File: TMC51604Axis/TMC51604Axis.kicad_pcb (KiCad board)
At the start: 4 copper layers, 77.7 x 72.8 mm, 162 parts, among them J1 +48Vin, J2 Stepper_conn, J3 RJ45_Shielded, J4 EncCon1, J5 RJ45_Shielded, J6 EncCon2, Q1 SUD08P06-155L, Q2 DMHT6016LFJ, Q3 DMHT6016LFJ, Q4 BSS138, U1 AP2210-3.3V, U2 LM2937, U3 TMC5160A-TA, U4 ASDMB-12.0MHz, U5 74LVC125, U6 74LVC125, U7 74LVC125

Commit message: First layout V2
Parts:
- removed C21, C39: 220uF/100V, Capacitor_SMD:CP_Elec_10x14.3
- removed C44, C45: 100n, peters:C_0805_peter
- removed D15: LED, peters:D_0805__HandSolder_peter
- removed D21, D22, D23, D24, D26, D29: BAT54S, Package_TO_SOT_SMD:SOT-23
- removed F1: Fuse, Fuse:Fuse_2512_6332Metric
- removed R47: 2k2, peters:R_0805_peter
- removed R49: 100R, peters:R_0805_peter
- removed R50: 20R, peters:R_0805_peter
- removed R51, R52: 0R1, Resistor_SMD:R_1206_3216Metric
- removed TP1, TP2: TestPoint, TestPoint:TestPoint_Pad_D1.5mm
- removed U6: 74LVC125, Package_SO:SO-14_5.3x10.2mm_P1.27mm
- added C50: 470n/100V, Capacitor_SMD:C_1206_3216Metric, F.Cu at (111.4, 116.5)
- added C51: 470n/100V, Capacitor_SMD:C_1206_3216Metric, F.Cu at (98.0, 116.5)
- added C52: 330uF/100V, Capacitor_THT:CP_Radial_D12.5mm_P5.00mm, F.Cu at (116.8, 126.9)
- added C53: 330uF/100V, Capacitor_THT:CP_Radial_D12.5mm_P5.00mm, F.Cu at (82.3, 113.9)
- added C54: 330uF/100V, Capacitor_THT:CP_Radial_D12.5mm_P5.00mm, F.Cu at (116.8, 113.6)
- added C55: 330uF/100V, Capacitor_THT:CP_Radial_D12.5mm_P5.00mm, F.Cu at (82.3, 127.3)
- added J7: Stepper_conn, Connector_Phoenix_MSTB:PhoenixContact_MSTBA_2,5_4-G-5,08_1x04_P5.08mm_Horizontal, F.Cu at (91.6, 124.5)
- added Q5: SQJ481EP, Libs:PowerPAK SO-8L SINGLE, B.Cu at (73.4, 121.8)
- added R53: 47K, Resistor_SMD:R_0603_1608Metric, B.Cu at (100.9, 85.6)
- added R54: 47K, Resistor_SMD:R_0603_1608Metric, B.Cu at (102.4, 85.6)
- added REF**: OSHW-Logo2_7.3x6mm_Copper, Symbol:OSHW-Logo2_7.3x6mm_Copper, F.Cu at (130.2, 117.2)
- C13, C14, D20, D25, D27, D28, R6: moved to F.Cu
- C15, C16: footprint Capacitor_SMD:C_1210_3225Metric_Pad1.42x2.65mm_HandSolder -> Capacitor_SMD:C_1210_3225Metric_Pad1.33x2.70mm_HandSolder; moved to B.Cu
- C18: footprint peters:C_0805_peter -> Capacitor_SMD:C_0603_1608Metric
- C19, C26, C27, D3, R10, R11, R13, R14, R22, R23, R24, R25, R3, R7, R8: moved to B.Cu
- C2: value 10p -> 100n; footprint peters:C_0805_peter -> Capacitor_SMD:C_0603_1608Metric; moved to B.Cu
- C20, C38: value 470n/100V -> 470n/100V x2
- C23: value 2.2uF -> 2.2uFto10uF
- C25: value 2.2u -> 2.2uFto10uF; moved to B.Cu
- C3, C4: footprint Capacitor_SMD:CP_Elec_8x6.2 -> Capacitor_SMD:CP_Elec_8x10
- C37: footprint peters:C_0805_peter -> peters:D_0805_peter
- C5: value 47nF -> 100n; footprint peters:C_0805_peter -> Capacitor_SMD:C_0603_1608Metric; moved to B.Cu
- C8: footprint Capacitor_SMD:C_2010_5025Metric_Pad1.52x2.65mm_HandSolder -> Capacitor_SMD:C_1210_3225Metric_Pad1.33x2.70mm_HandSolder
- D11, D12, D13, D14, D16, D17, D18, D19: value LED -> BAT54S; footprint peters:D_0805__HandSolder_peter -> Package_TO_SOT_SMD:SOT-23
- D6: value D_Schottky -> SS34FA
- FB2: footprint Resistor_SMD:R_0805_2012Metric_Pad1.15x1.40mm_HandSolder -> Resistor_SMD:R_0805_2012Metric_Pad1.20x1.40mm_HandSolder
- J3: value RJ45_Shielded -> RJ45_STEP_DIR
- J5: value RJ45_Shielded -> RJ45_SPI
- JP1, JP2: footprint Jumper:SolderJumper-3_P2.0mm_Open_TrianglePad1.0x1.5mm -> Jumper:SolderJumper-3_P1.3mm_Bridged12_RoundedPad1.0x1.5mm
- Q1: value SUD08P06-155L -> BSS138; footprint Package_TO_SOT_SMD:TO-252-2 -> Package_TO_SOT_SMD:SOT-23
- Q2, Q3: value DMHT6016LFJ -> DMHT6016LFJ-Peters; footprint Libs:V-DFN5045-12 -> Libs:V-DFN5045-12 (Type B)
- R1: value 0R01 -> 100R; footprint Resistor_SMD:R_2512_6332Metric -> peters:R_0805_peter; moved to B.Cu
- R16, R27: value 0R1 -> 0R05; footprint Resistor_SMD:R_1206_3216Metric -> Resistor_SMD:R_2512_6332Metric_Pad1.40x3.35mm_HandSolder
- R19: footprint peters:R_0805_peter -> Resistor_SMD:R_0603_1608Metric
- R31, R32: value 2k2 -> 100R; moved to B.Cu
- R41: value 2k2 -> R; footprint peters:R_0805_peter -> peters:C_0805_peter; moved to B.Cu
- R42, R43, R44: value 2k2 -> 100K; footprint peters:R_0805_peter -> Resistor_SMD:R_0603_1608Metric
- R45, R46: value 2k2 -> 10K; footprint peters:R_0805_peter -> Resistor_SMD:R_0603_1608Metric
- TP4, TP5, TP6: footprint TestPoint:TestPoint_Pad_1.5x1.5mm -> TestPoint:TestPoint_THTPad_D1.0mm_Drill0.5mm
- U7: value 74LVC125 -> TXB0108PWR; footprint Package_SO:SO-14_5.3x10.2mm_P1.27mm -> digikey-footprints:TSSOP-20_W4.4mm
- moved H4 95.9 mm to (134.6, 65.2)
- moved JP1 80.9 mm to (73.3, 66.1), turned to 0 degrees
- moved H3 70.4 mm to (64.0, 65.2)
- moved R39 70.4 mm to (127.0, 74.7), turned to 0 degrees
- moved JP2 69.3 mm to (84.3, 66.1), turned to 0 degrees
- moved JP3 66.7 mm to (95.4, 66.1)
- moved J3 66.4 mm to (133.1, 97.2)
- moved J4 66.3 mm to (109.8, 66.3)
- moved J6 66.2 mm to (121.3, 66.3)
- moved J5 66.1 mm to (133.2, 78.1)
- moved H1 65.8 mm to (63.9, 131.0)
- moved C42 62.1 mm to (98.8, 65.5), turned to 180 degrees
- moved R38 60.9 mm to (110.0, 69.6), turned to 90 degrees
- moved C46 60.0 mm to (126.8, 105.3), turned to 180 degrees
- moved R48 59.6 mm to (114.3, 69.6)
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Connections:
- net Net-(C32-Pad1) renamed /MotorDrv1/SRB-
- net Net-(C32-Pad2) renamed /MotorDrv1/SRB+
- net Net-(C40-Pad1) renamed /MotorDrv1/SRA-
- net Net-(C40-Pad2) renamed /MotorDrv1/SRA+
- C2 pad 1: +48V -> GND
- C2 pad 2: Net-(C2-Pad2) -> VBUS
- C5 pad 1: Net-(C2-Pad2) -> GND
- C5 pad 2: GND -> +3V3
- D11 pad 2: Net-(D11-Pad2) -> VBUS
- D12 pad 2: Net-(D12-Pad2) -> VBUS
- D13 pad 2: Net-(D13-Pad2) -> VBUS
- D14 pad 2: Net-(D14-Pad2) -> VBUS
- D16 pad 1: Net-(D16-Pad1) -> GND
- D16 pad 2: /Inputs/DIR_REFR -> VBUS
- D17 pad 1: Net-(D17-Pad1) -> GND
- D17 pad 2: /MotorDrv1/REFL_STEP -> VBUS
- D18 pad 1: Net-(D18-Pad1) -> GND
- D18 pad 2: Net-(D18-Pad2) -> VBUS
- D19 pad 1: Net-(D19-Pad1) -> GND
- D19 pad 2: Net-(D19-Pad2) -> VBUS
- D20 pad 2: /Inputs/Signal_VCC -> VBUS
- D20 pad 3: Net-(D20-Pad3) -> /Inputs/SCK_raw
- D25 pad 3: Net-(D25-Pad3) -> /Inputs/ENC_A_raw
- D27 pad 3: Net-(D27-Pad3) -> /Inputs/ENC_B_raw
- D28 pad 3: Net-(D28-Pad3) -> /Inputs/ENC_N_raw
- D3 pad 1: Net-(C2-Pad2) -> +48V
- D5 pad 13: (no net) -> Net-(D5-Pad13)
- D5 pad 15: (no net) -> Net-(D5-Pad15)
- D5 pad 3: (no net) -> Net-(D5-Pad3)
- D5 pad 5: (no net) -> Net-(D5-Pad5)
- D5 pad 7: (no net) -> Net-(D5-Pad7)
- J2 pad 1: /MotorDrv1/StepperA -> /MotorDrv1/StepperD
- J2 pad 2: /MotorDrv1/StepperB -> /MotorDrv1/StepperC
- J2 pad 3: /MotorDrv1/StepperC -> /MotorDrv1/StepperB
- J2 pad 4: /MotorDrv1/StepperD -> /MotorDrv1/StepperA
- J3 pad 1: GND -> Net-(J3-Pad1)
- J3 pad 3: GND -> Net-(J3-Pad3)
- J3 pad 4: Net-(J3-Pad4) -> GND
- J3 pad 5: GND -> Net-(J3-Pad5)
- J3 pad 6: Net-(J3-Pad6) -> GND
- J3 pad 7: GND -> Net-(J3-Pad7)
- J3 pad 8: Net-(J3-Pad8) -> VBUS
- J4 pad 1: /Inputs/ENC_B_raw -> Net-(J4-Pad1)
- J4 pad 2: /Inputs/ENC_A_raw -> Net-(J4-Pad2)
- J5 pad 1: GND -> Net-(J5-Pad1)
- J5 pad 2: /Inputs/CSN_raw -> GND
- J5 pad 3: GND -> Net-(J5-Pad3)
- J5 pad 4: /Inputs/SDI_raw -> GND
- J5 pad 5: GND -> Net-(J5-Pad5)
- J5 pad 6: /Inputs/SDO_raw -> GND
- J5 pad 7: GND -> Net-(J5-Pad7)
- J5 pad 8: /Inputs/SCK_raw -> GND
- J6 pad 3: /Inputs/ENC_N_raw -> Net-(J6-Pad3)
- JP1 pad 1: GND -> +3V3
- JP1 pad 2: Net-(JP1-Pad2) -> /MotorDrv1/SPI_MODE
- JP1 pad 3: +3V3 -> GND
- JP2 pad 1: GND -> +3V3
- JP2 pad 2: Net-(JP2-Pad2) -> /MotorDrv1/SD_MODE
- JP2 pad 3: +3V3 -> GND
- Q1 pad 1: Net-(D3-Pad2) -> Net-(Q1-Pad1)
- Q1 pad 2: Net-(F1-Pad1) -> GND
- Q1 pad 3: Net-(C2-Pad2) -> Net-(Q1-Pad3)
- Q2 pad 10: /MotorDrv1/StepperB -> /MotorDrv1/StepperD
- Q2 pad 14: /MotorDrv1/StepperA -> /MotorDrv1/StepperC
- Q2 pad 15: /MotorDrv1/StepperB -> /MotorDrv1/StepperD
- Q2 pad 3: /MotorDrv1/StepperA -> /MotorDrv1/StepperC
- Q2 pad 5: Net-(C33-Pad2) -> Net-(C41-Pad2)
- Q2 pad 6: Net-(C33-Pad2) -> Net-(C41-Pad2)
- Q2 pad 7: Net-(C33-Pad2) -> Net-(C41-Pad2)
- Q2 pad 8: Net-(C33-Pad2) -> Net-(C41-Pad2)
- Q3 pad 10: /MotorDrv1/StepperD -> /MotorDrv1/StepperB
- Q3 pad 14: /MotorDrv1/StepperC -> /MotorDrv1/StepperA
- Q3 pad 15: /MotorDrv1/StepperD -> /MotorDrv1/StepperB
- Q3 pad 3: /MotorDrv1/StepperC -> /MotorDrv1/StepperA
- Q3 pad 5: Net-(C41-Pad2) -> Net-(C33-Pad2)
- Q3 pad 6: Net-(C41-Pad2) -> Net-(C33-Pad2)
- Q3 pad 7: Net-(C41-Pad2) -> Net-(C33-Pad2)
- Q3 pad 8: Net-(C41-Pad2) -> Net-(C33-Pad2)
- Q4 pad 2: GND -> Net-(Q1-Pad3)
- R1 pad 1: Net-(C2-Pad2) -> /Inputs/DIR_raw
- R1 pad 2: +48V -> Net-(J3-Pad7)
- R10 pad 2: Net-(Q2-Pad1) -> Net-(Q3-Pad1)
- R11 pad 1: Net-(Q2-Pad12) -> Net-(Q3-Pad12)
- R13 pad 2: Net-(Q2-Pad4) -> Net-(Q3-Pad4)
- R14 pad 1: Net-(Q2-Pad9) -> Net-(Q3-Pad9)
- R22 pad 2: Net-(Q3-Pad1) -> Net-(Q2-Pad1)
- R23 pad 1: Net-(Q3-Pad12) -> Net-(Q2-Pad12)
- R24 pad 2: Net-(Q3-Pad4) -> Net-(Q2-Pad4)
- R25 pad 1: Net-(Q3-Pad9) -> Net-(Q2-Pad9)
- R31 pad 1: /MotorDrv1/CLK -> /Inputs/Step_Raw
- R31 pad 2: Net-(D11-Pad2) -> Net-(J3-Pad5)
- R32 pad 1: /MotorDrv1/MOSI -> /MotorDrv1/DRV_ENA
- R32 pad 2: Net-(D12-Pad2) -> Net-(J3-Pad3)
- R33 pad 1: Net-(D20-Pad3) -> /Inputs/DIAG1_SWp_OUT
- R33 pad 2: Net-(J3-Pad4) -> Net-(J3-Pad2)
- R34 pad 1: Net-(D21-Pad3) -> /Inputs/DIAG0_SWn_OUT
- R34 pad 2: /Inputs/SDO_raw -> Net-(J3-Pad1)
- R35 pad 1: Net-(D22-Pad3) -> /Inputs/SCK_raw
- R35 pad 2: /Inputs/CSN_raw -> Net-(J5-Pad7)
- R36 pad 1: Net-(D23-Pad3) -> /Inputs/SDO_raw
- R36 pad 2: /Inputs/SDI_raw -> Net-(J5-Pad5)
- R37 pad 1: Net-(D24-Pad3) -> /Inputs/SDI_raw
- R37 pad 2: /Inputs/SCK_raw -> Net-(J5-Pad3)
- R38 pad 1: Net-(D25-Pad3) -> /Inputs/ENC_B_raw
- R38 pad 2: /Inputs/ENC_A_raw -> Net-(J4-Pad1)
- R39 pad 1: Net-(D26-Pad3) -> /Inputs/CSN_raw
- R39 pad 2: Net-(J3-Pad8) -> Net-(J5-Pad1)
- R40 pad 1: Net-(D27-Pad3) -> Net-(J4-Pad2)
- R40 pad 2: /Inputs/ENC_B_raw -> /Inputs/ENC_A_raw
- R41 pad 1: /Inputs/CSN -> Net-(R41-Pad1)
- R41 pad 2: Net-(D13-Pad2) -> GND
- R42 pad 1: /MotorDrv1/MISO -> Net-(Q1-Pad1)
- R42 pad 2: Net-(D14-Pad2) -> +12V
- R43 pad 1: Net-(D15-Pad1) -> GND
- R43 pad 2: GND -> Net-(Q1-Pad1)
- R44 pad 1: Net-(D16-Pad1) -> +3V3
- R44 pad 2: GND -> Net-(Q1-Pad3)
- R45 pad 1: Net-(D17-Pad1) -> +3V3
- R45 pad 2: GND -> /Inputs/DIR_REFR
- R46 pad 1: Net-(D18-Pad1) -> +3V3
- R46 pad 2: GND -> /MotorDrv1/REFL_STEP
- R48 pad 1: Net-(D28-Pad3) -> Net-(J6-Pad3)
- U3 pad 15: /MotorDrv1/MOSI -> /Inputs/SDI
- U3 pad 16: /MotorDrv1/MISO -> /Inputs/SDO
- U3 pad 21: Net-(JP1-Pad2) -> /MotorDrv1/SD_MODE
- U3 pad 22: Net-(JP2-Pad2) -> /MotorDrv1/SPI_MODE
- U3 pad 26: /MotorDrv1/DIAG0_SWn -> /Inputs/DIAG0_SWn
- U3 pad 27: /MotorDrv1/DIAG1_SWp -> /Inputs/DIAG1_SWp
- U5 pad 11: Net-(D19-Pad2) -> (no net)
- U5 pad 12: /MotorDrv1/DIAG0_SWn -> (no net)
- U5 pad 13: GND -> (no net)
- U7 pad 1: GND -> /Inputs/DIAG1_SWp
- U7 pad 10: GND -> Net-(R41-Pad1)
- U7 pad 11: Net-(D18-Pad2) -> GND
- U7 pad 12: /MotorDrv1/DIAG1_SWp -> /Inputs/SCK_raw
- U7 pad 13: GND -> /Inputs/SDO_raw
- U7 pad 14: +3V3 -> /Inputs/SDI_raw
- U7 pad 2: Net-(D20-Pad3) -> +3V3
- U7 pad 3: /MotorDrv1/DRV_ENA -> /Inputs/DIAG0_SWn
- U7 pad 4: GND -> /MotorDrv1/REFL_STEP
- U7 pad 5: Net-(D26-Pad3) -> /Inputs/DIR_REFR
- U7 pad 6: /Inputs/DIR_REFR -> /Inputs/CSN
- U7 pad 7: GND -> /Inputs/SDI
- U7 pad 8: /MotorDrv1/REFL_STEP -> /Inputs/SDO
- U7 pad 9: Net-(D29-Pad3) -> /MotorDrv1/CLK
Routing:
- net GND: track 353.8 -> 157.7 mm, vias 119 -> 288
- net +3V3: track 44.0 -> 148.4 mm, vias 15 -> 14
- net /Inputs/Signal_VCC: track 87.6 -> 0.00 mm, vias 7 -> 0
- net VBUS: track 0.00 -> 86.1 mm, vias 0 -> 9
- net +5V: track 107.5 -> 41.7 mm, vias 3 -> 2
- net /MotorDrv1/SPI_MODE: track 0.00 -> 64.2 mm, vias 0 -> 2
- net /MotorDrv1/SD_MODE: track 0.00 -> 56.1 mm, vias 0 -> 2
- net Net-(JP1-Pad2): track 45.5 -> 0.00 mm, vias 2 -> 0
- net Net-(JP2-Pad2): track 41.2 -> 0.00 mm, vias 2 -> 0
- net /MotorDrv1/SRA-: track 43.6 -> 11.3 mm, vias 2 -> 0
- net /MotorDrv1/MOSI: track 31.6 -> 0.00 mm, vias 2 -> 0
- net Net-(D29-Pad3): track 31.4 -> 0.00 mm
- net /MotorDrv1/HB1: track 14.0 -> 44.2 mm, vias 2 -> 1
- net /Inputs/DIR_raw: track 0.00 -> 29.1 mm, vias 0 -> 1
- net Net-(D19-Pad2): track 28.5 -> 0.00 mm, vias 2 -> 0
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- added copper zone on B.Cu, net +12V
- added copper zone on In2.Cu, net +48V
- added copper zone on F.Cu, net /MotorDrv1/StepperA
- added copper zone on In1.Cu, net /MotorDrv1/StepperA
- added copper zone on In2.Cu, net /MotorDrv1/StepperA
- added copper zone on F.Cu, net /MotorDrv1/StepperB
- added copper zone on In1.Cu, net /MotorDrv1/StepperB
- added copper zone on In2.Cu, net /MotorDrv1/StepperB
- added copper zone on F.Cu, net /MotorDrv1/StepperC
- added copper zone on In1.Cu, net /MotorDrv1/StepperC
- added copper zone on In2.Cu, net /MotorDrv1/StepperC
- added copper zone on F.Cu, net /MotorDrv1/StepperD
- added copper zone on In1.Cu, net /MotorDrv1/StepperD
- added copper zone on In2.Cu, net /MotorDrv1/StepperD
- added copper zone on B.Cu, net Net-(C1-Pad2)
- added copper zone on In2.Cu, net Net-(J1-Pad2)
- removed copper zone on In2.Cu, net +3V3
- removed copper zone on F.Cu, net Net-(C2-Pad2)
- removed copper zone on B.Cu, net Net-(C33-Pad2)
- removed copper zone on B.Cu, net Net-(C41-Pad2)
- removed copper zone on F.Cu, net Net-(F1-Pad1)
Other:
- board size 77.7 x 72.8 mm -> 77.7 x 72.7 mm
- net class +12V added: clearance 0.2, trace_width 0.4, via_dia 0.6, via_drill 0.4
- net class +3V3 added: clearance 0.2, trace_width 0.4, via_dia 0.45, via_drill 0.2
- net class +5V added: clearance 0.2, trace_width 0.4, via_dia 0.45, via_drill 0.2
- net class Default: via_dia 0.6 -> 0.45; via_drill 0.3 -> 0.2
- rule via_min_drill: 0.3 -> 0.2
- board text added: "MAX 60VDC 5A"
- board text added: "NC"
- board text added: "SPI RJ45 CSN: ORG/WHT SDI: GRN/WHT SDO: BLU/WHT SCK: BRN/WHT"
- board text added: "STEP/DIR"
- board text added: "Step/Dir"
- board text added: "Step/Dir RJ45 Diag0: ORG/WHT Diag1: ORG DRVEna: GRN/WHT Step: BLU/WHT Dir: BRN/WHT VBUS: BRN"
- board text added: "TMC5160 Stepper Driver v2"
- board text removed: "+48VDC IN"
- board text removed: "CSN"
- board text removed: "DIAG_SWn"
- board text removed: "DIAG_SWp"
- board text removed: "DIR_REF_R"
- board text removed: "ENA"
- board text removed: "GND"
- board text removed: "SCK"
- board text removed: "SDI"
- board text removed: "SDO"
- board text removed: "SPI IN"
- board text removed: "STEP/DIR IN"
- board text removed: "STEP_REF_L"
- board text removed: "See TMC5160 datasheet for SD_MODE and SPI_MODE CFG page 13"
- board text removed: "TMC5160 Stepper Driver 48V 6A MAX"

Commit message: cleanup
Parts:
- removed REF**: OSHW-Logo2_7.3x6mm_Copper, Symbol:OSHW-Logo2_7.3x6mm_Copper
- C15, C16: footprint Capacitor_SMD:C_1210_3225Metric_Pad1.33x2.70mm_HandSolder -> Capacitor_SMD:C_1206_3216Metric
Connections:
- U5 pad 11: (no net) -> GND
- U5 pad 12: (no net) -> GND
- U5 pad 13: (no net) -> GND
- U5 pad 5: /Inputs/ENC_A_raw -> /Inputs/ENC_A
- U5 pad 6: /Inputs/ENC_A -> /Inputs/ENC_A_raw
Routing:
- net GND: track 157.7 -> 163.4 mm, vias 288 -> 291
- net /Inputs/ENC_A_raw: track 14.9 -> 13.6 mm
- net /Inputs/ENC_A: track 22.7 -> 22.0 mm

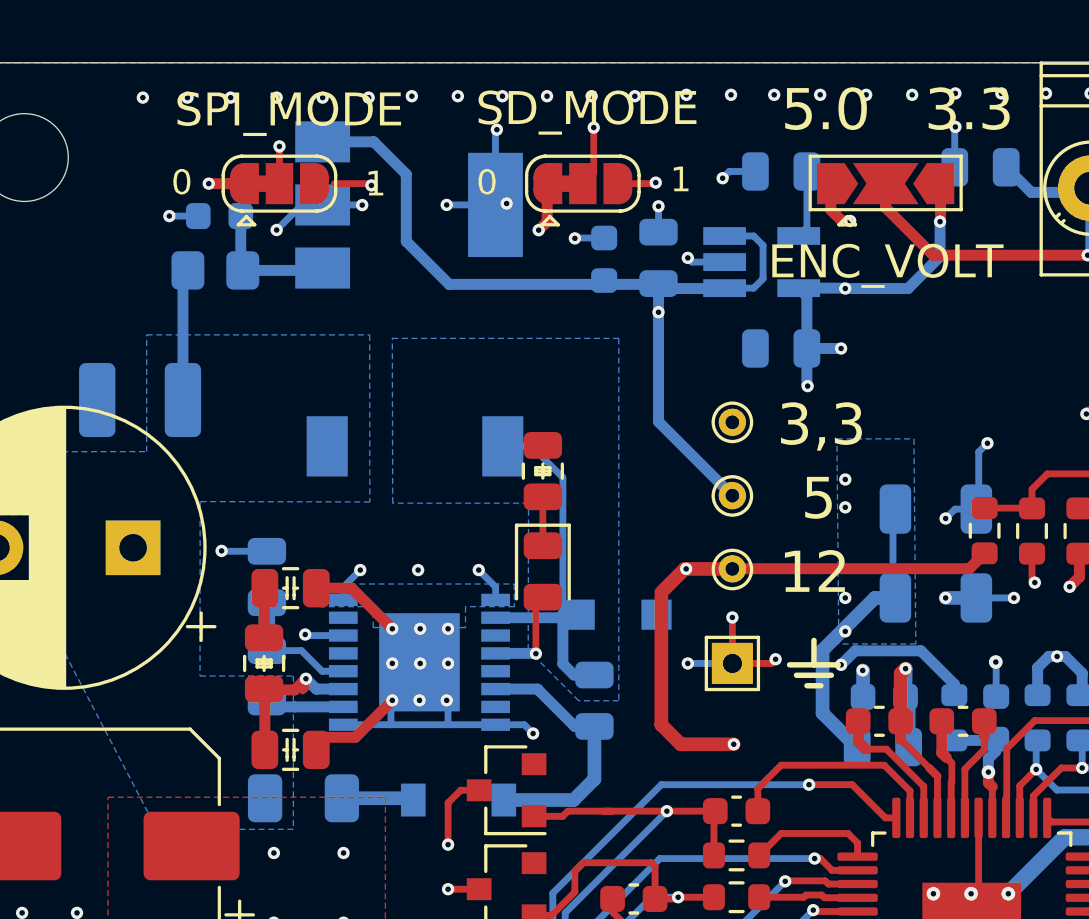
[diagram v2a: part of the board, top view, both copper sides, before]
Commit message: correced silk top
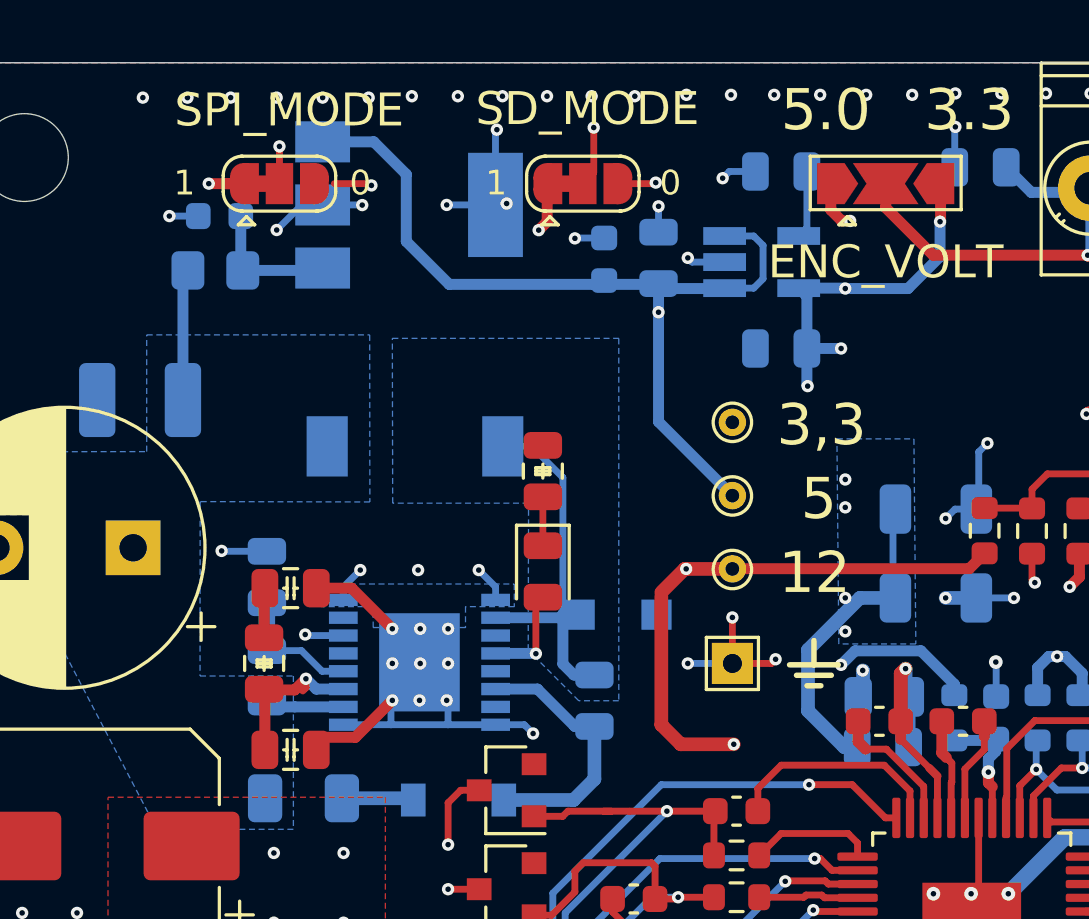
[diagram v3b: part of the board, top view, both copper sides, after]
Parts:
- C19: footprint Capacitor_SMD:C_0603_1608Metric -> Capacitor_SMD:C_0805_2012Metric
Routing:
- net +48V: track 66.2 -> 67.2 mm

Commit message: sync
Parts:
- D10, D7, D8, D9: value ZHCS1006TA -> Min60V 1A; footprint Package_TO_SOT_SMD:SOT-23 -> Diode_SMD:D_SOD-123
- R1, R31, R32, R33, R34, R35, R36, R37, R38, R39, R40, R48: footprint peters:R_0805_peter -> Resistor_SMD:R_0603_1608Metric
- R12, R20, R21, R9: moved to B.Cu
- R41: value R -> 62K
- U5: footprint Package_SO:SO-14_5.3x10.2mm_P1.27mm -> Package_SO:SO-14_3.9x8.65mm_P1.27mm
- moved D8 11.8 mm to (84.3, 87.6)
- moved D9 10.7 mm to (84.3, 98.6)
- moved C22 4.19 mm to (90.2, 93.7), turned to 0 degrees
- moved C36 4.11 mm to (90.2, 91.6), turned to 0 degrees
- moved D10 2.79 mm to (84.3, 91.3)
- moved D7 2.78 mm to (84.3, 94.9)
- moved C24 1.68 mm to (90.2, 96.1)
- moved R21 1.48 mm to (89.7, 89.2)
- moved R12 0.80 mm to (89.7, 93.9)
- moved R20 0.68 mm to (89.7, 91.5)
- moved C35 0.50 mm to (90.2, 89.4)
- moved R41 0.31 mm to (117.3, 83.8), turned to 270 degrees
- moved R9 0.26 mm to (89.7, 96.2)
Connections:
- D10 pad 1: /MotorDrv1/StepperC -> Net-(D10-Pad1)
- D10 pad 2: (no net) -> GND
- D7 pad 1: /MotorDrv1/StepperB -> Net-(D7-Pad1)
- D7 pad 2: (no net) -> GND
- D8 pad 1: /MotorDrv1/StepperA -> Net-(D8-Pad1)
- D8 pad 2: (no net) -> GND
- D9 pad 1: /MotorDrv1/StepperD -> Net-(D9-Pad1)
- D9 pad 2: (no net) -> GND
- R12 pad 1: Net-(R12-Pad1) -> Net-(D7-Pad1)
- R20 pad 1: Net-(R20-Pad1) -> Net-(D10-Pad1)
- R21 pad 1: Net-(R21-Pad1) -> Net-(D8-Pad1)
- R41 pad 1: Net-(R41-Pad1) -> +3V3
- R41 pad 2: GND -> Net-(R41-Pad2)
- R9 pad 1: Net-(R9-Pad1) -> Net-(D9-Pad1)
- U3 pad 37: Net-(R21-Pad1) -> Net-(D8-Pad1)
- U3 pad 40: Net-(R20-Pad1) -> Net-(D10-Pad1)
- U3 pad 45: Net-(R12-Pad1) -> Net-(D7-Pad1)
- U3 pad 48: Net-(R9-Pad1) -> Net-(D9-Pad1)
- U5 pad 11: GND -> Net-(U5-Pad11)
- U7 pad 10: Net-(R41-Pad1) -> Net-(R41-Pad2)
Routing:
- net /MotorDrv1/StepperC: track 39.5 -> 6.36 mm, vias 8 -> 7
- net Net-(D10-Pad1): track 0.00 -> 11.7 mm, vias 0 -> 1
- net Net-(D9-Pad1): track 0.00 -> 11.1 mm, vias 0 -> 2
- net Net-(D7-Pad1): track 0.00 -> 10.8 mm, vias 0 -> 2
- net Net-(D8-Pad1): track 0.00 -> 10.7 mm, vias 0 -> 2
- net GND: track 163.4 -> 154.1 mm, vias 291 -> 287
- net /MotorDrv1/StepperB: track 42.9 -> 36.1 mm, vias 8 -> 7
- net Net-(C22-Pad2): track 9.63 -> 3.36 mm
- net Net-(C36-Pad2): track 9.61 -> 4.54 mm
- net Net-(C25-Pad1): track 29.4 -> 24.7 mm
- net /MotorDrv1/StepperA: track 45.8 -> 41.2 mm
- net /MotorDrv1/StepperD: track 52.2 -> 47.7 mm
- net Net-(R21-Pad1): track 4.56 -> 0.00 mm
- net Net-(R9-Pad1): track 4.52 -> 0.00 mm
- net Net-(R12-Pad1): track 3.71 -> 0.00 mm
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- added copper zone on F.Cu, net (none)

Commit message: sync
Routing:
- net /MotorDrv1/StepperC: track 6.36 -> 33.0 mm, vias 7 -> 9
- net /MotorDrv1/StepperB: track 36.1 -> 38.8 mm, vias 7 -> 8
- net +3V3: track 150.2 -> 152.9 mm
- net Net-(R41-Pad2): track 0.00 -> 1.54 mm
- net /MotorDrv1/HA1: track 35.9 -> 35.3 mm
